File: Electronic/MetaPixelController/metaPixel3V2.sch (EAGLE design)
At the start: 3 parts, among them IC1 74HC245N

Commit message: fixing include stuff
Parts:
- added JP1: (no value), pinhead:PINHD-1X1
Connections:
- removed net !MEM_CS: U$1.6
- removed net !SD_CS: U$1.10
- removed net A_BCLK: U$1.9
- removed net A_LRCLK: U$1.23/A9
- removed net A_MCLK: U$1.11
- removed net A_RX: U$1.13
- removed net A_TX: U$1.22/A8
- removed net SCL: U$1.19/A5
- removed net SDA: U$1.18/A4
- net !LCD_CS: now also U$1.10; no longer U$1.20/A6
- net LCD_DC: now also U$1.9; no longer U$1.15/A1
- net LCD_LED: now also JP1.1; no longer U$1.3
- net MOSI: now also U$1.11; no longer U$1.7
- net SCLK: now also U$1.13; no longer U$1.14/A0

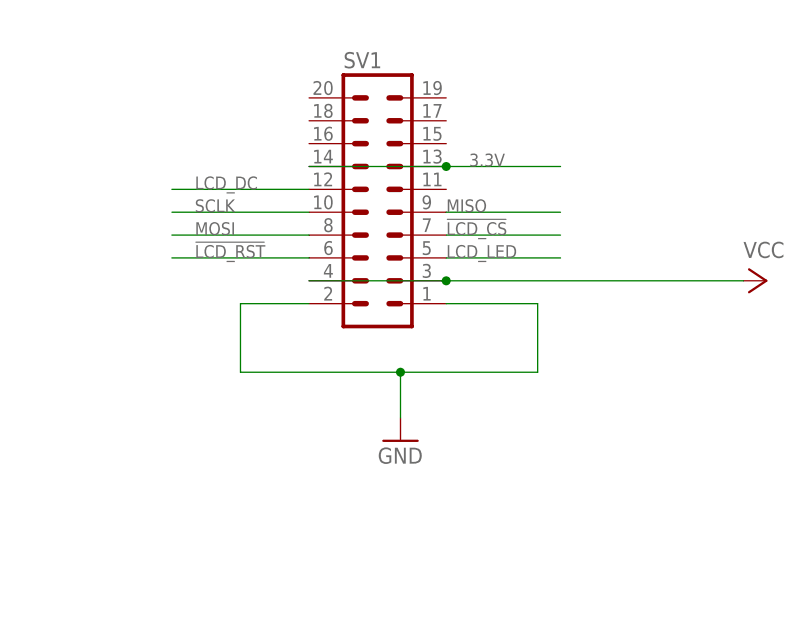
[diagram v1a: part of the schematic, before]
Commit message: Updated connectors
and more work on the UI Boards
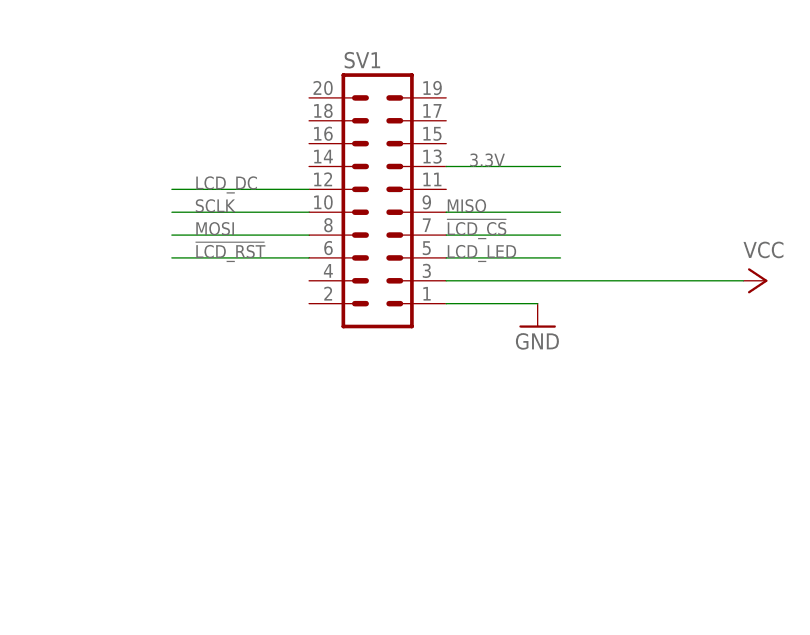
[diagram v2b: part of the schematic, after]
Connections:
- net 3.3V: no longer SV1.14
- net GND: no longer SV1.2
- net VCC: no longer SV1.4
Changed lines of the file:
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@@
 <?xml version="1.0" encoding="utf-8"?>
 <!DOCTYPE eagle SYSTEM "eagle.dtd">
-<eagle version="7.4.0">
+<eagle version="7.4.1">
 <drawing>
 <settings>
@@
 <grid distance="0.1" unitdist="inch" unit="inch" style="lines" multiple="1" display="no" altdistance="0.01" altunitdist="inch" altunit="inch"/>
 <layers>
-<layer number="1" name="Top" color="4" fill="1" visible="yes" active="no"/>
-<layer number="2" name="Route2" color="1" fill="3" visible="yes" active="no"/>
-<layer number="15" name="Route15" color="4" fill="6" visible="yes" active="no"/>
-<layer number="16" name="Bottom" color="1" fill="1" visible="yes" active="no"/>
-<layer number="17" name="Pads" color="2" fill="1" visible="yes" active="no"/>
-<layer number="18" name="Vias" color="2" fill="1" visible="yes" active="no"/>
-<layer number="19" name="Unrouted" color="6" fill="1" visible="yes" active="no"/>
-<layer number="20" name="Dimension" color="15" fill="1" visible="yes" active="no"/>
-<layer number="21" name="tPlace" color="7" fill="1" visible="yes" active="no"/>
-<layer number="22" name="bPlace" color="7" fill="1" visible="yes" active="no"/>
-<layer number="23" name="tOrigins" color="15" fill="1" visible="yes" active="no"/>
-<layer number="24" name="bOrigins" color="15" fill="1" visible="yes" active="no"/>
-<layer number="25" name="tNames" color="7" fill="1" visible="yes" active="no"/>
-<layer number="26" name="bNames" color="7" fill="1" visible="yes" active="no"/>
-<layer number="27" name="tValues" color="7" fill="1" visible="yes" active="no"/>
-<layer number="28" name="bValues" color="7" fill="1" visible="yes" active="no"/>
+<layer number="1" name="Top" color="4" fill="1" visible="no" active="no"/>
+<layer number="2" name="Route2" color="1" fill="3" visible="no" active="no"/>
+<layer number="15" name="Route15" color="4" fill="6" visible="no" active="no"/>
+<layer number="16" name="Bottom" color="1" fill="1" visible="no" active="no"/>
+<layer number="17" name="Pads" color="2" fill="1" visible="no" active="no"/>
+<layer number="18" name="Vias" color="2" fill="1" visible="no" active="no"/>
+<layer number="19" name="Unrouted" color="6" fill="1" visible="no" active="no"/>
+<layer number="20" name="Dimension" color="15" fill="1" visible="no" active="no"/>
+<layer number="21" name="tPlace" color="7" fill="1" visible="no" active="no"/>
+<layer number="22" name="bPlace" color="7" fill="1" visible="no" active="no"/>
+<layer number="23" name="tOrigins" color="15" fill="1" visible="no" active="no"/>
+<layer number="24" name="bOrigins" color="15" fill="1" visible="no" active="no"/>
+<layer number="25" name="tNames" color="7" fill="1" visible="no" active="no"/>
+<layer number="26" name="bNames" color="7" fill="1" visible="no" active="no"/>
+<layer number="27" name="tValues" color="7" fill="1" visible="no" active="no"/>
+<layer number="28" name="bValues" color="7" fill="1" visible="no" active="no"/>
 <layer number="29" name="tStop" color="7" fill="3" visible="no" active="no"/>
 <layer number="30" name="bStop" color="7" fill="6" visible="no" active="no"/>
@@
 <layer number="35" name="tGlue" color="7" fill="4" visible="no" active="no"/>
 <layer number="36" name="bGlue" color="7" fill="5" visible="no" active="no"/>
-<layer number="37" name="tTest" color="7" fill="1" visible="yes" active="no"/>
-<layer number="38" name="bTest" color="7" fill="1" visible="yes" active="no"/>
+<layer number="37" name="tTest" color="7" fill="1" visible="no" active="no"/>
+<layer number="38" name="bTest" color="7" fill="1" visible="no" active="no"/>
 <layer number="39" name="tKeepout" color="4" fill="11" visible="no" active="no"/>
 <layer number="40" name="bKeepout" color="1" fill="11" visible="no" active="no"/>
@@
 <layer number="44" name="Drills" color="7" fill="1" visible="no" active="no"/>
 <layer number="45" name="Holes" color="7" fill="1" visible="no" active="no"/>
-<layer number="46" name="Milling" color="3" fill="1" visible="yes" active="no"/>
-<layer number="47" name="Measures" color="7" fill="1" visible="yes" active="no"/>
-<layer number="48" name="Document" color="7" fill="1" visible="yes" active="no"/>
-<layer number="49" name="Reference" color="7" fill="1" visible="yes" active="no"/>
-<layer number="51" name="tDocu" color="7" fill="1" visible="yes" active="no"/>
-<layer number="52" name="bDocu" color="7" fill="1" visible="yes" active="no"/>
+<layer number="46" name="Milling" color="3" fill="1" visible="no" active="no"/>
+<layer number="47" name="Measures" color="7" fill="1" visible="no" active="no"/>
+<layer number="48" name="Document" color="7" fill="1" visible="no" active="no"/>
+<layer number="49" name="Reference" color="7" fill="1" visible="no" active="no"/>
+<layer number="51" name="tDocu" color="7" fill="1" visible="no" active="no"/>
+<layer number="52" name="bDocu" color="7" fill="1" visible="no" active="no"/>
 <layer number="90" name="Modules" color="5" fill="1" visible="yes" active="yes"/>
 <layer number="91" name="Nets" color="2" fill="1" visible="yes" active="yes"/>
@@
 <instances>
 <instance part="U$1" gate="G$1" x="38.1" y="43.18"/>
-<instance part="GND1" gate="1" x="144.78" y="17.78"/>
+<instance part="GND1" gate="1" x="160.02" y="30.48"/>
 <instance part="P+1" gate="VCC" x="185.42" y="35.56" rot="R270"/>
 <instance part="P+2" gate="VCC" x="68.58" y="58.42" rot="R270"/>
@@
 <net name="GND" class="0">
 <segment>
-<wire x1="134.62" y1="33.02" x2="127" y2="33.02" width="0.1524" layer="91"/>
-<wire x1="127" y1="33.02" x2="127" y2="25.4" width="0.1524" layer="91"/>
-<wire x1="127" y1="25.4" x2="144.78" y2="25.4" width="0.1524" layer="91"/>
-<wire x1="144.78" y1="25.4" x2="160.02" y2="25.4" width="0.1524" layer="91"/>
-<wire x1="160.02" y1="25.4" x2="160.02" y2="33.02" width="0.1524" layer="91"/>
-<wire x1="160.02" y1="33.02" x2="149.86" y2="33.02" width="0.1524" layer="91"/>
-<wire x1="144.78" y1="25.4" x2="144.78" y2="20.32" width="0.1524" layer="91"/>
-<junction x="144.78" y="25.4"/>
-<pinref part="GND1" gate="1" pin="GND"/>
-<pinref part="SV1" gate="1" pin="1"/>
-<pinref part="SV1" gate="1" pin="2"/>
-</segment>
-<segment>
 <pinref part="IC1" gate="A" pin="G"/>
 <wire x1="83.82" y1="-40.64" x2="71.12" y2="-40.64" width="0.1524" layer="91"/>
 <pinref part="GND2" gate="1" pin="GND"/>
 </segment>
+<segment>
+<wire x1="160.02" y1="33.02" x2="149.86" y2="33.02" width="0.1524" layer="91"/>
+<pinref part="SV1" gate="1" pin="1"/>
+<pinref part="GND1" gate="1" pin="GND"/>
+</segment>
 </net>
 <net name="VCC" class="0">
@@
 <segment>
 <pinref part="P+1" gate="VCC" pin="VCC"/>
-<wire x1="134.62" y1="35.56" x2="149.86" y2="35.56" width="0.1524" layer="91"/>
 <pinref part="SV1" gate="1" pin="3"/>
 <wire x1="149.86" y1="35.56" x2="182.88" y2="35.56" width="0.1524" layer="91"/>
-<junction x="149.86" y="35.56"/>
-<pinref part="SV1" gate="1" pin="4"/>
 </segment>
 </net>
@@
 </segment>
 <segment>
-<wire x1="134.62" y1="48.26" x2="149.86" y2="48.26" width="0.1524" layer="91"/>
 <label x="152.4" y="48.26" size="1.4224" layer="95"/>
 <pinref part="SV1" gate="1" pin="13"/>
 <wire x1="149.86" y1="48.26" x2="162.56" y2="48.26" width="0.1524" layer="91"/>
-<junction x="149.86" y="48.26"/>
-<pinref part="SV1" gate="1" pin="14"/>
-</segment>
-</net>
+</segment>
+</net>

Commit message: The first 3 Boards are ready
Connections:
- removed net N$1: IC1A.A2
- removed net N$2: IC1A.A3
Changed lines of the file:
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@@
-</segment>
-</net>
-<net name="N$1" class="0">
-<segment>
-<pinref part="IC1" gate="A" pin="A2"/>
-<wire x1="83.82" y1="-17.78" x2="68.58" y2="-17.78" width="0.1524" layer="91"/>
-</segment>
-</net>
-<net name="N$2" class="0">
-<segment>
-<pinref part="IC1" gate="A" pin="A3"/>
-<wire x1="83.82" y1="-20.32" x2="68.58" y2="-20.32" width="0.1524" layer="91"/>
 </segment>
 </net>
